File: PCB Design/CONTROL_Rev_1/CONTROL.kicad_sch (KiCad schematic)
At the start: 46 parts, among them J1 Conn_01x24_Pin, J2 Conn_01x24_Pin, J3 Micro_SD_Card, J4 USB_C_Receptacle_USB2.0_16P, SW1 SW_SPDT, U1 STM32F446RET6, Y1 16MHz, Y2 32.768KHz

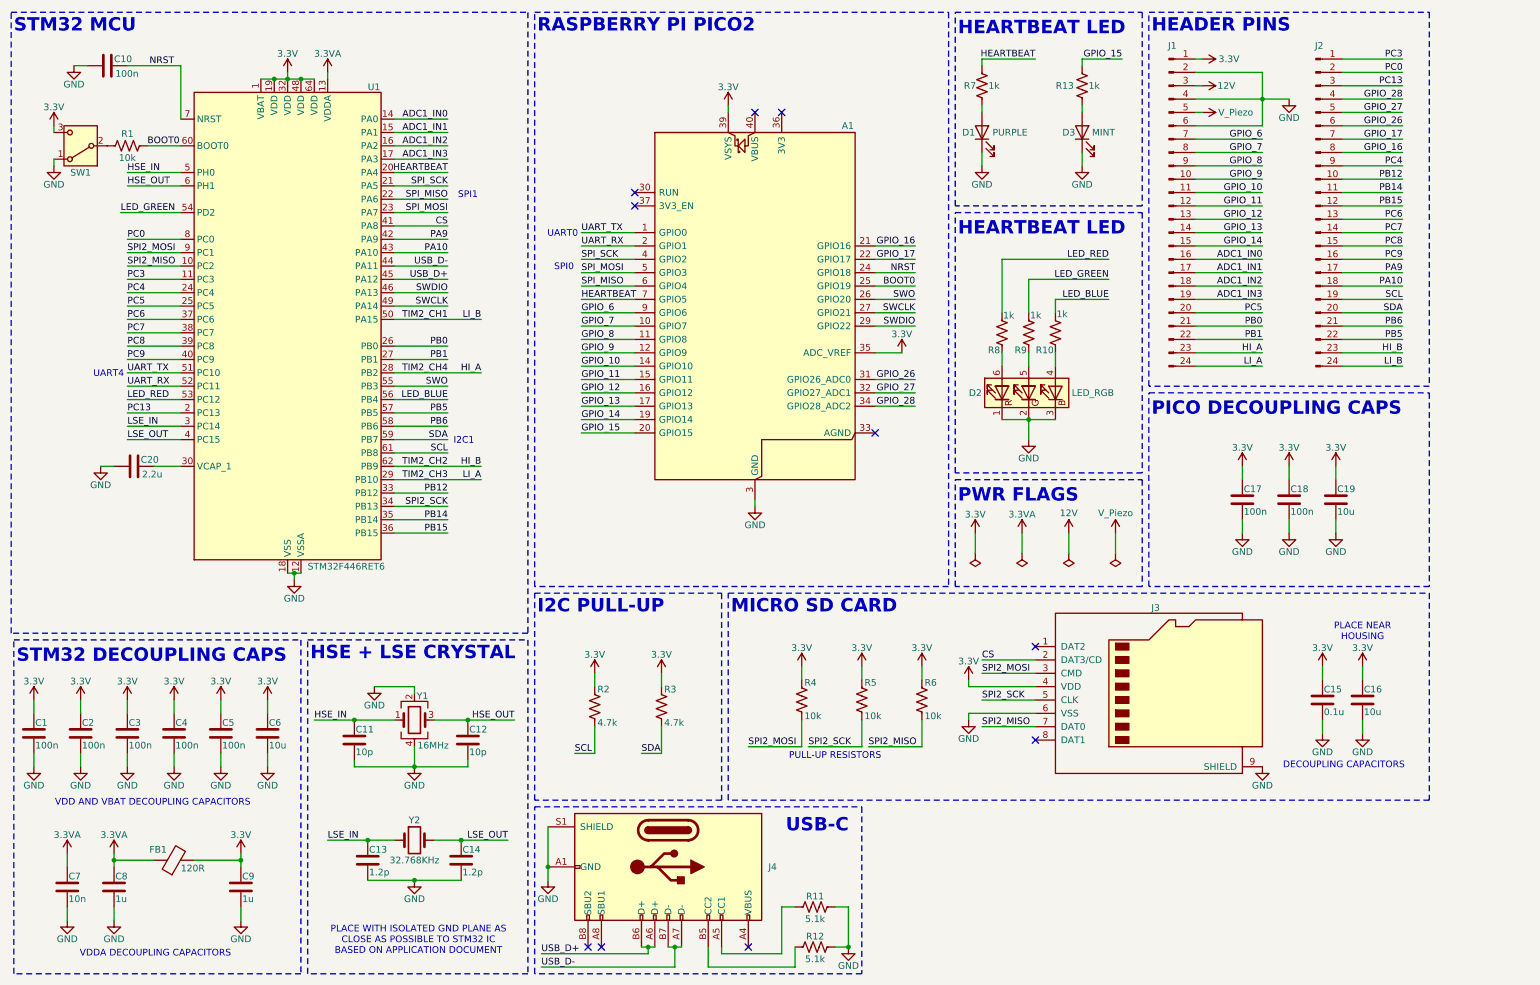
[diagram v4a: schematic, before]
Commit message: fix(usb-c): add ESD protection and clean up VBUS handling
- Add USBLC6-2SC6 TVS diode array on D+ and D- (J4)
- Add 100k bleed resistor from VBUS to GND (VBUS not powered)
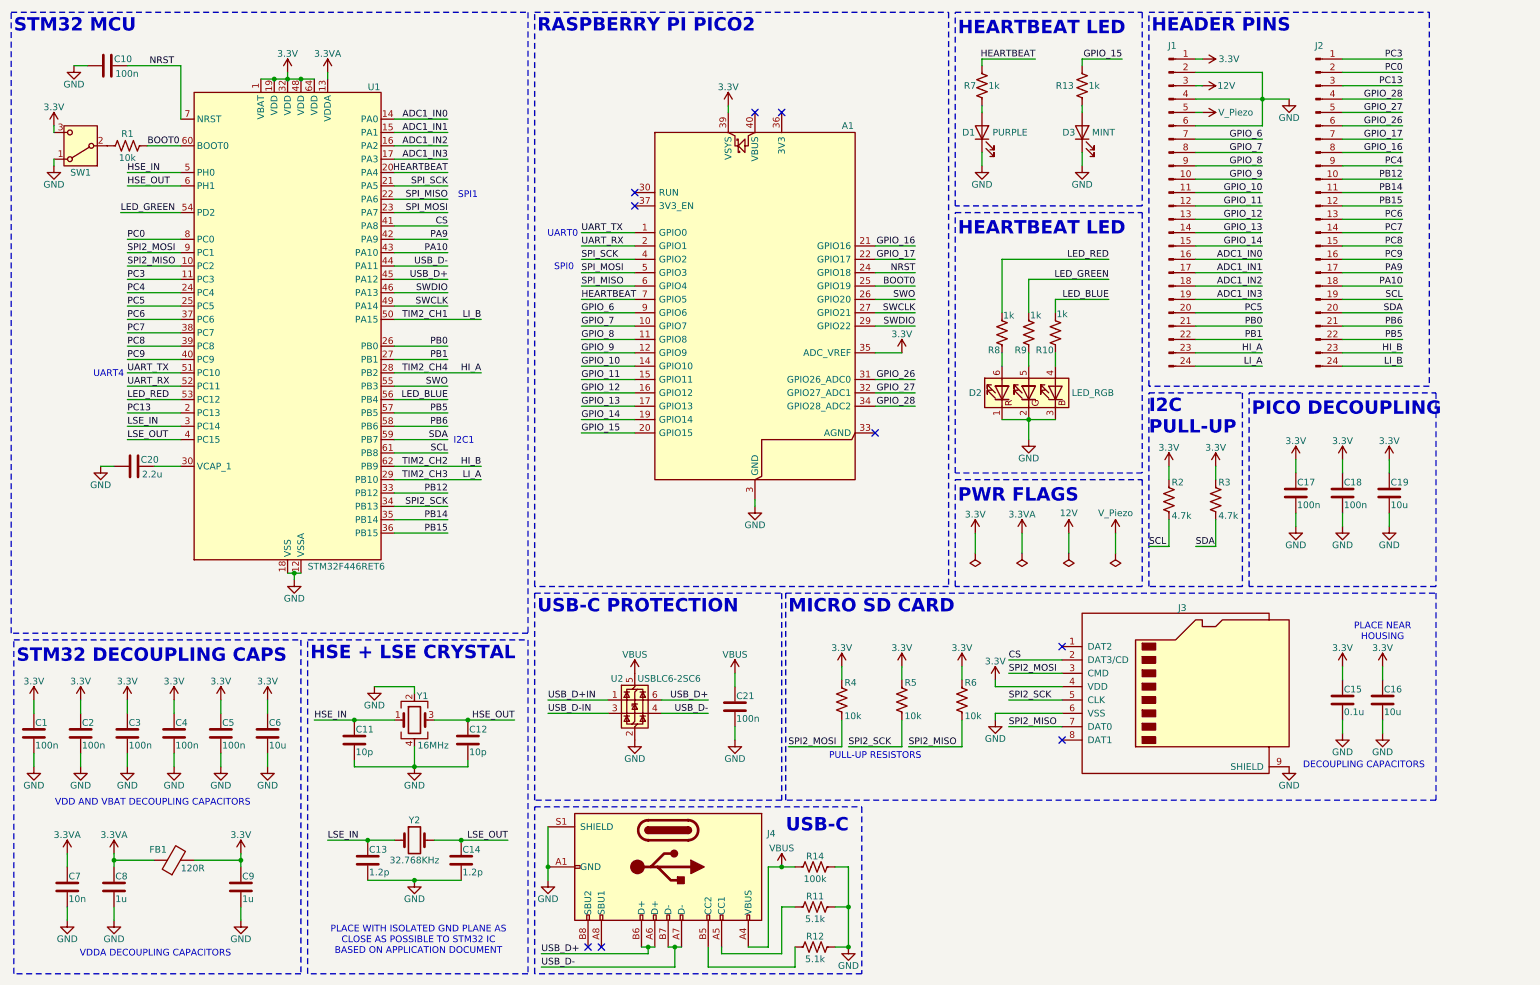
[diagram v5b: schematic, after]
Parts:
- added C21: 100n, Capacitor_SMD:C_0603_1608Metric, symbol Device:C
- added R14: 100k, Resistor_SMD:R_0603_1608Metric, symbol Device:R_US
- added U2: USBLC6-2SC6, Package_TO_SOT_SMD:SOT-23-6, symbol Power_Protection:USBLC6-2SC6
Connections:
- net GND: now also C21.2, R14.2, U2.2 (GND)
- net USB_D+: now also U2.6 (I/O1)
- net USB_D-: now also U2.4 (I/O2)
- net VBUS: now reaches J4.A4 (VBUS), J4.A9 (VBUS), J4.B4 (VBUS), J4.B9 (VBUS)
- net VBUS: now also C21.1, R14.1, U2.5 (VBUS)
- new net USB_D+IN: U2.1 (I/O1)
- new net USB_D-IN: U2.3 (I/O2)
- no-connect marks 10 -> 9
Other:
- note added: "PICO DECOUPLING"
- note added: "USB-C PROTECTION"
- note removed: "PICO DECOUPLING CAPS"
- moved on the sheet: C15, C16, C17, C18, C19, J3, R2, R3, R4, R5, R6

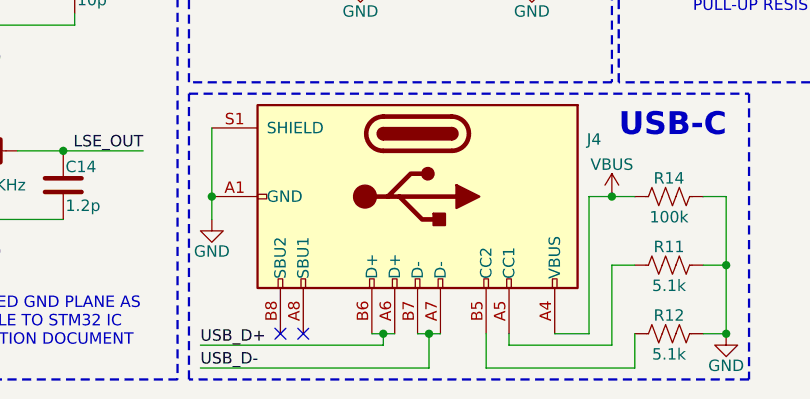
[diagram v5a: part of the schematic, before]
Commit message: Updated USB Port Schematic and PCB
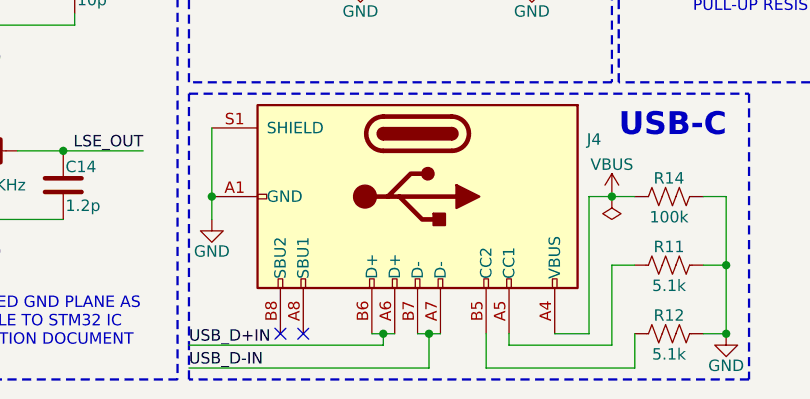
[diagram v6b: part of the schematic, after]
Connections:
- net USB_D+: no longer J4.A6 (D+), J4.B6 (D+)
- net USB_D+IN: now also J4.A6 (D+), J4.B6 (D+)
- net USB_D-: no longer J4.A7 (D-), J4.B7 (D-)
- net USB_D-IN: now also J4.A7 (D-), J4.B7 (D-)
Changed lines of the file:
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@@
 	(wire
 		(pts
-			(xy 114.3 193.04) (xy 134.62 193.04)
+			(xy 113.03 193.04) (xy 134.62 193.04)
 		)
 		(stroke
@@
 	(wire
 		(pts
-			(xy 114.3 195.58) (xy 139.7 195.58)
+			(xy 113.03 195.58) (xy 139.7 195.58)
 		)
 		(stroke
@@
 		)
 	)
-	(label "USB_D+"
-		(at 114.3 193.04 0)
+	(label "USB_D+IN"
+		(at 113.03 193.04 0)
 		(effects
 			(font
@@
 		)
 	)
-	(label "USB_D-"
-		(at 114.3 195.58 0)
+	(label "USB_D-IN"
+		(at 113.03 195.58 0)
 		(effects
 			(font
@@
 					(unit 1)
 				)
+			)
+		)
+	)
+	(symbol
+		(lib_id "power:PWR_FLAG")
+		(at 160.02 176.53 180)
+		(unit 1)
+		(exclude_from_sim no)
+		(in_bom yes)
+		(on_board yes)
+		(dnp no)
+		(property "Reference" "#FLG05"
+			(at 160.02 178.435 0)
+			(effects
+				(font
+					(size 1.27 1.27)
+				)
+				(hide yes)
+			)
+		)
+		(property "Value" "PWR_FLAG"
+			(at 160.02 180.594 0)
+			(effects
+				(font
+					(size 1.27 1.27)
+				)
+				(hide yes)
+			)
+		)
+		(property "Footprint" ""
+			(at 160.02 176.53 0)
+			(effects
+				(font
+					(size 1.27 1.27)
+				)
+				(hide yes)
+			)
+		)
+		(property "Datasheet" "~"
+			(at 160.02 176.53 0)
+			(effects
+				(font
+					(size 1.27 1.27)
+				)
+				(hide yes)
+			)
+		)
+		(property "Description" "Special symbol for telling ERC where power comes from"
+			(at 160.02 176.53 0)
+			(effects
+				(font
+					(size 1.27 1.27)
+				)
+				(hide yes)
+			)
+		)
+		(pin "1"
+		)
+		(instances
+			(project "CONTROL"
+				(path "/0692d2c3-ddc7-44ef-a4e6-56d2a9ee62f1"
+					(reference "#FLG05")
+					(unit 1)
+				)

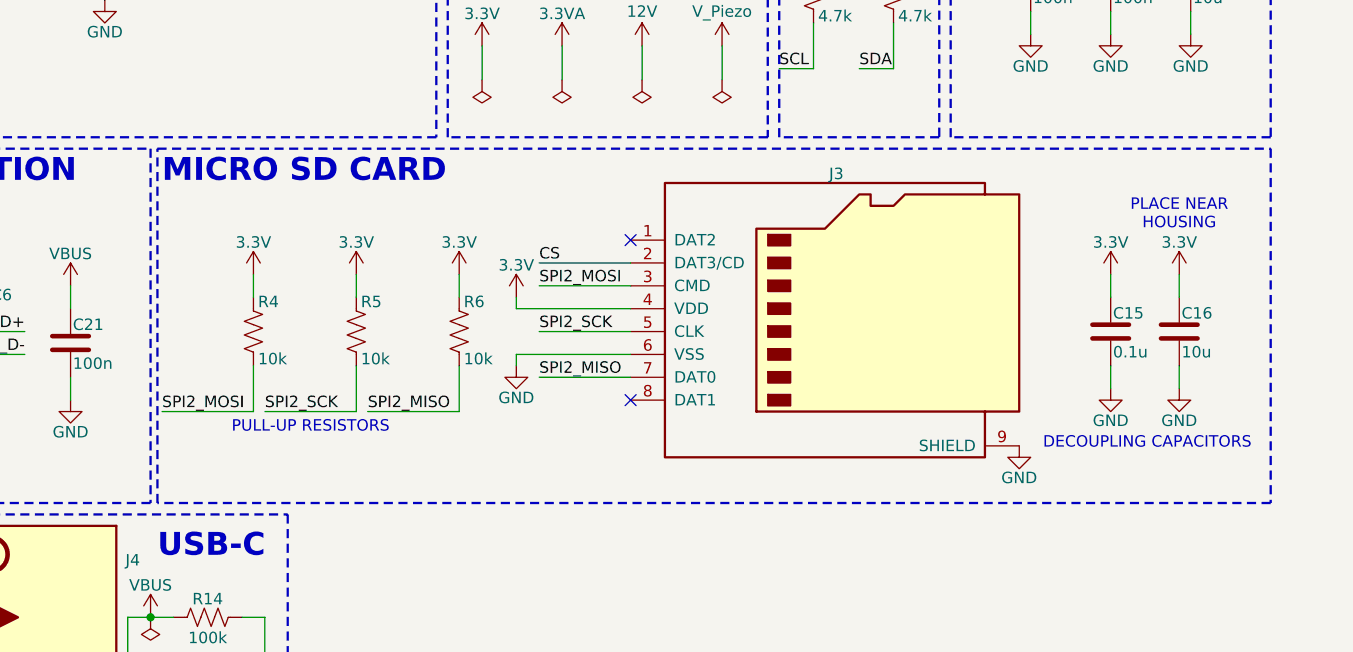
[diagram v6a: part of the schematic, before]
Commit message: fix(sd-card): pull up unused DAT1 and DAT2 lines
- Add 47k pull-up resistors on DAT1 (pin 8) and DAT2 (pin 1) to 3.3V
- Required by SD spec to prevent undefined bus state during init
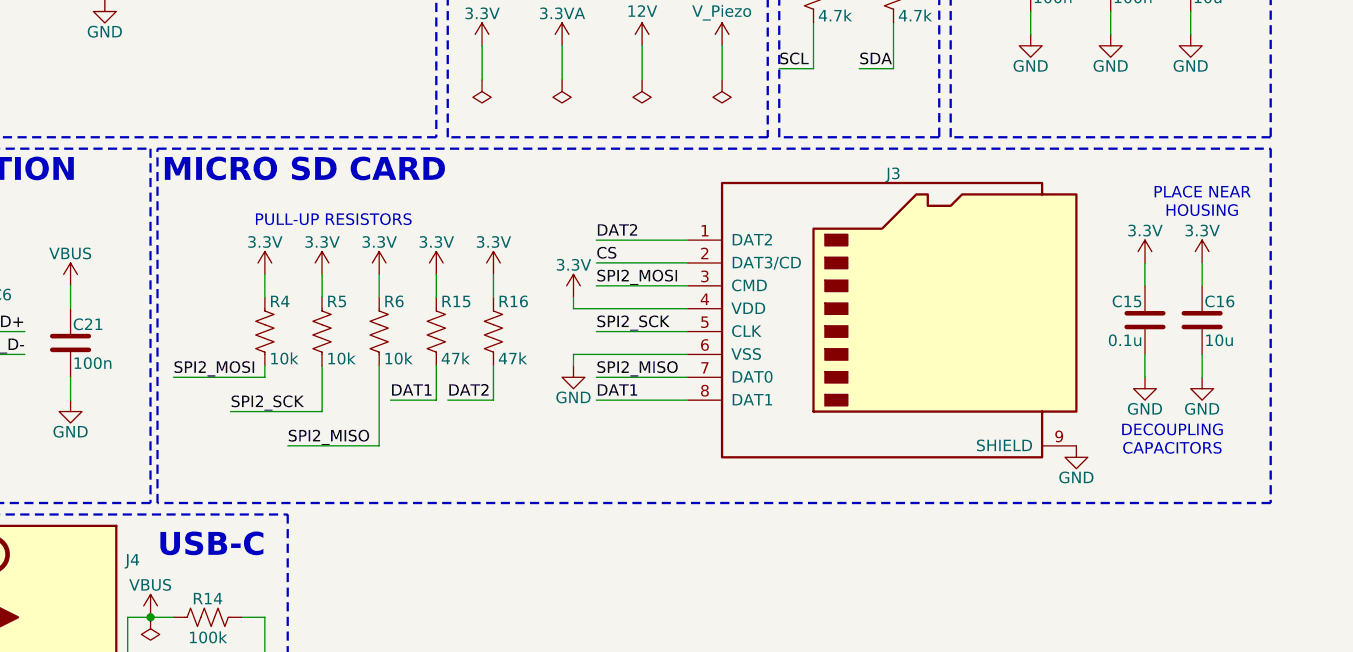
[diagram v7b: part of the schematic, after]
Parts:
- added R15, R16: 47k, Resistor_SMD:R_0603_1608Metric, symbol Device:R_US
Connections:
- net 3.3V: now also R15.1, R16.1
- net DAT2: now reaches J3.1 (DAT2)
- net DAT2: now also R16.2
- net DAT1: now reaches J3.8 (DAT1)
- net DAT1: now also R15.2
- no-connect marks 9 -> 7
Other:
- moved on the sheet: C15, C16, J3, R4, R5, R6

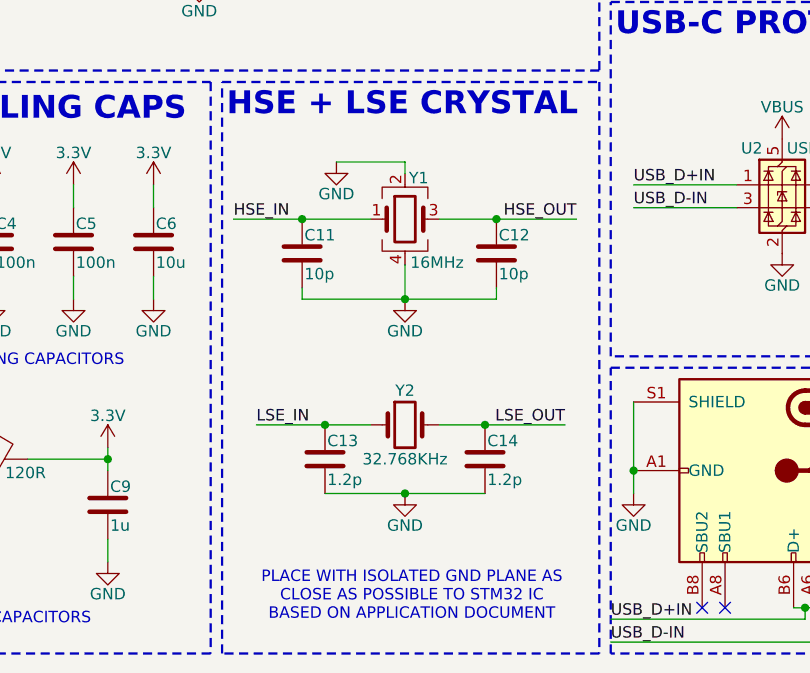
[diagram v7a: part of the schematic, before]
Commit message: fix(crystals): correct LSE load cap configuration
- Remove C13 and C14 (1.2pF external load caps on LSE)
- ABS05W has CL = 4pF; use STM32 internal OSC caps instead
- HSE caps C11/C12 confirmed correct at 10pF for E3SB16E (CL = 8pF)
- Note: configure LSE drive to low-power mode in firmware to match ABS05W ESR
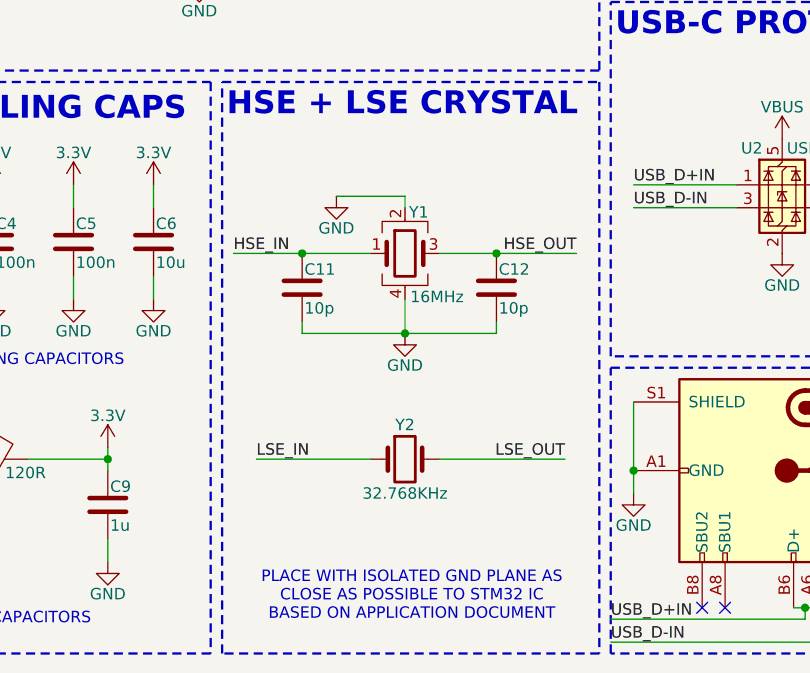
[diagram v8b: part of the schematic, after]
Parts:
- removed C13, C14: 1.2p, Capacitor_SMD:C_0402_1005Metric, symbol Device:C
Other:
- moved on the sheet: C11, C12, Y1, Y2
